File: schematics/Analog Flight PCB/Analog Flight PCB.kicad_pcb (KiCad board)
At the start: 2 copper layers, 99.1 x 56.4 mm, 79 parts, among them J1 Conn_01x02_Male, J10 Conn_01x02_Male, J11 Conn_01x02_Male, J12 Conn_01x02_Male, J2 Conn_01x03_Male, J3 Conn_01x03_Male, J4 Conn_01x03_Male, J5 Conn_01x05_Male, J6 Conn_01x02_Male, J7 Conn_01x02_Male, J8 Conn_01x02_Male, J9 Conn_02x06_Top_Bottom, U1 MAX31856, U2 ADS1115IDGS, U3 NAU7802SGI, U4 MAX31856, U5 MAX31856, U6 MAX31856, U7 MAX31856, U8 MAX31856, U9 LP2985-3.3

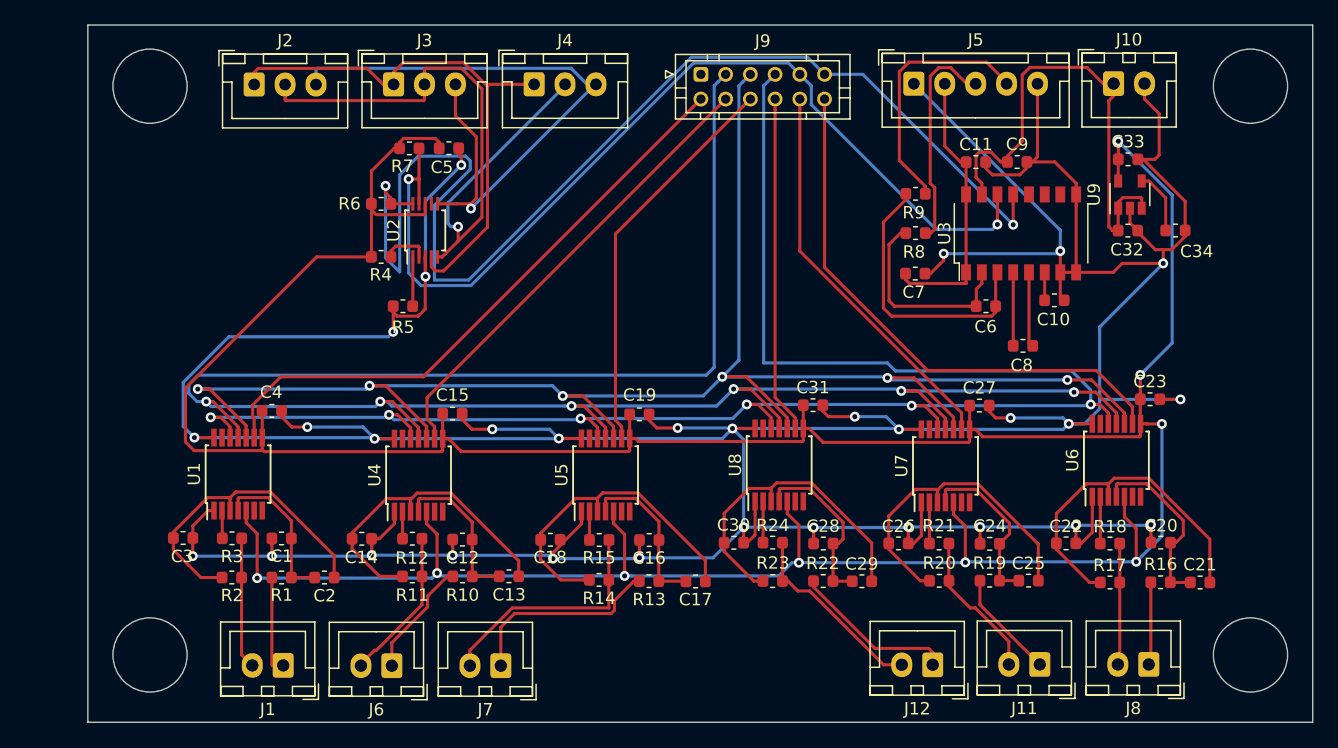
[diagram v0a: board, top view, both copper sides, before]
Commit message: ASPCB: Revision 1.0c
Changed all single row plug connectors to JST-PH instead of JST-XH to
save space. All routes were optimized to place passives closer to ICs
and contacts. Two additional LC reader assemblies were added for test
config. Testpoints have been added on both 3v3 and 5v power supplies for
testing. Power and ground have been moved into primary connector, with
interleaving to preserve signal integrity. First attempt at a ground
plane was implemented. Graphics have been added to silkscreen, and
date/revision info have been added to silkscreen. Parts have been
renumbered for clarity where applicable.
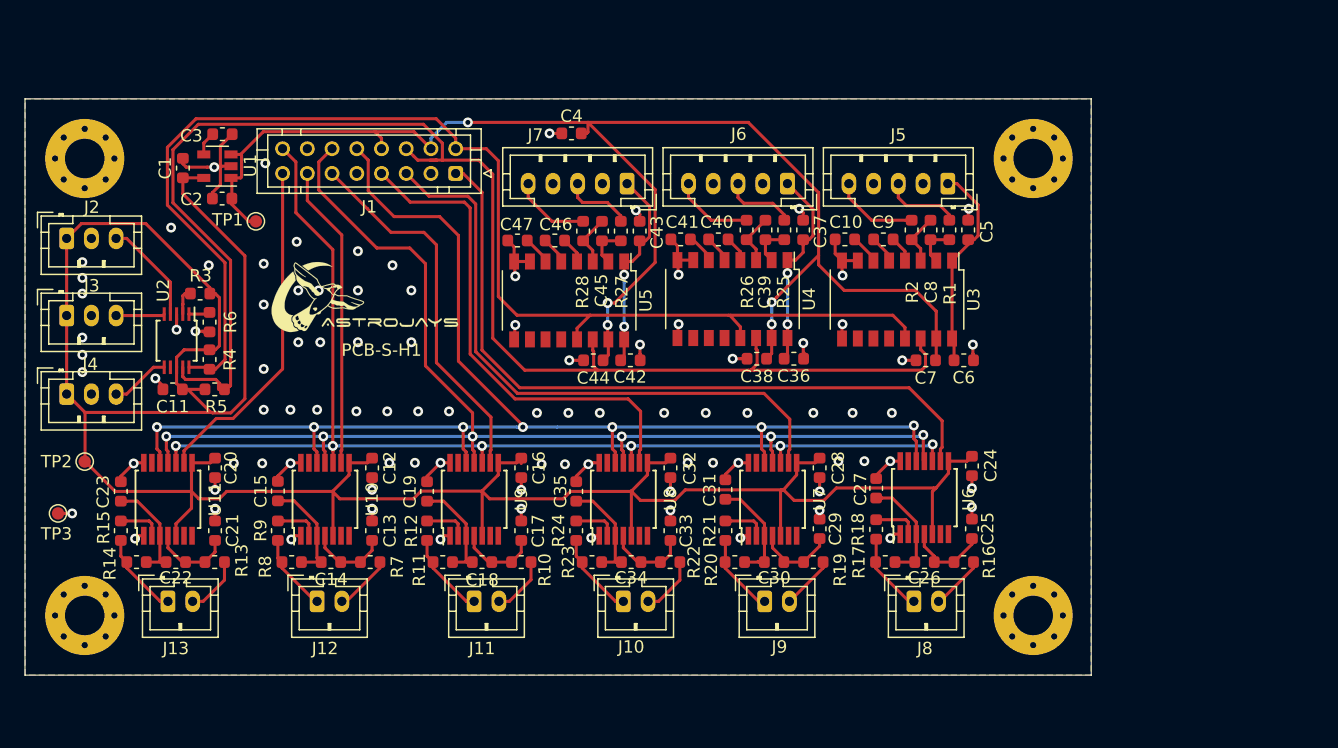
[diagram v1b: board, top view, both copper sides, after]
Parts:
- removed the J10 at (176.4, 71.8)
- removed the J9 at (143.1, 71.0)
- added C36: 0.1u, Capacitor_SMD:C_0603_1608Metric, F.Cu at (150.6, 94.0)
- added C37: 1u, Capacitor_SMD:C_0603_1608Metric, F.Cu at (151.3, 83.6)
- added C38: 1u, Capacitor_SMD:C_0603_1608Metric, F.Cu at (147.6, 94.0)
- added C39: 0.1u, Capacitor_SMD:C_0603_1608Metric, F.Cu at (148.3, 83.6)
- added C4: 10u, Capacitor_SMD:C_0603_1608Metric, F.Cu at (132.6, 75.8)
- added C40: 680p, Capacitor_SMD:C_0603_1608Metric, F.Cu at (144.5, 84.4)
- added C41: 0.1u, Capacitor_SMD:C_0603_1608Metric, F.Cu at (141.4, 84.4)
- added C42: 0.1u, Capacitor_SMD:C_0603_1608Metric, F.Cu at (137.3, 94.2)
- added C43: 1u, Capacitor_SMD:C_0603_1608Metric, F.Cu at (138.1, 83.7)
- added C44: 1u, Capacitor_SMD:C_0603_1608Metric, F.Cu at (134.4, 94.2)
- added C45: 0.1u, Capacitor_SMD:C_0603_1608Metric, F.Cu at (135.1, 83.7)
- added C46: 680p, Capacitor_SMD:C_0603_1608Metric, F.Cu at (131.2, 84.5)
- added C47: 0.1u, Capacitor_SMD:C_0603_1608Metric, F.Cu at (128.2, 84.5)
- added G***: LOGO, AJ_GFX:full_logo_21.3mmx9.3mm, F.Cu at (117.5, 88.8)
- added G***: LOGO, AJ_GFX:small_logo_5.71mmx5.71mm, B.Cu at (152.8, 106.8)
- added J1: Conn_02x08_Odd_Even, Connector_JST:JST_PHD_B16B-PHDSS_2x08_P2.00mm_Vertical, F.Cu at (123.2, 79.1)
- added J6: Conn_01x05_Male, Connector_JST:JST_PH_B5B-PH-K_1x05_P2.00mm_Vertical, F.Cu at (150.1, 79.9)
- added J7: Conn_01x05_Male, Connector_JST:JST_PH_B5B-PH-K_1x05_P2.00mm_Vertical, F.Cu at (137.1, 79.9)
- added M1: MountingHole_3.2mm_M3_Pad_Via, MountingHole:MountingHole_3.2mm_M3_Pad_Via, F.Cu at (93.2, 114.8)
- added M2: MountingHole_3.2mm_M3_Pad_Via, MountingHole:MountingHole_3.2mm_M3_Pad_Via, F.Cu at (93.2, 77.9)
- added M3: MountingHole_3.2mm_M3_Pad_Via, MountingHole:MountingHole_3.2mm_M3_Pad_Via, F.Cu at (169.9, 77.9)
- added M4: MountingHole_3.2mm_M3_Pad_Via, MountingHole:MountingHole_3.2mm_M3_Pad_Via, F.Cu at (169.9, 114.8)
- added R25: 47, Resistor_SMD:R_0603_1608Metric, F.Cu at (149.8, 83.6)
- added R26: 47, Resistor_SMD:R_0603_1608Metric, F.Cu at (146.7, 83.6)
- added R27: 47, Resistor_SMD:R_0603_1608Metric, F.Cu at (136.6, 83.7)
- added R28: 47, Resistor_SMD:R_0603_1608Metric, F.Cu at (133.5, 83.7)
- added TP1: TestPoint, TestPoint:TestPoint_Pad_D1.0mm, F.Cu at (107.1, 82.9)
- added TP2: TestPoint, TestPoint:TestPoint_Pad_D1.0mm, F.Cu at (93.2, 102.4)
- added TP3: TestPoint, TestPoint:TestPoint_Pad_D1.0mm, F.Cu at (91.1, 106.6)
- added U4: NAU7802SGI, Package_SO:SOP-16_4.4x10.4mm_P1.27mm, F.Cu at (145.6, 89.2)
- added U5: NAU7802SGI, Package_SO:SOP-16_4.4x10.4mm_P1.27mm, F.Cu at (132.4, 89.3)
- J10: renamed from J7; footprint Connector_JST:JST_XH_B2B-XH-A_1x02_P2.50mm_Vertical -> Connector_JST:JST_PH_B2B-PH-K_1x02_P2.00mm_Vertical
- J11: renamed from J8; footprint Connector_JST:JST_XH_B2B-XH-A_1x02_P2.50mm_Vertical -> Connector_JST:JST_PH_B2B-PH-K_1x02_P2.00mm_Vertical
- J12: renamed from J11; footprint Connector_JST:JST_XH_B2B-XH-A_1x02_P2.50mm_Vertical -> Connector_JST:JST_PH_B2B-PH-K_1x02_P2.00mm_Vertical
- J13: renamed from J12; footprint Connector_JST:JST_XH_B2B-XH-A_1x02_P2.50mm_Vertical -> Connector_JST:JST_PH_B2B-PH-K_1x02_P2.00mm_Vertical
- J2, J3, J4: footprint Connector_JST:JST_XH_B3B-XH-A_1x03_P2.50mm_Vertical -> Connector_JST:JST_PH_B3B-PH-K_1x03_P2.00mm_Vertical
- J5: footprint Connector_JST:JST_XH_B5B-XH-A_1x05_P2.50mm_Vertical -> Connector_JST:JST_PH_B5B-PH-K_1x05_P2.00mm_Vertical
- J8: renamed from J1; footprint Connector_JST:JST_XH_B2B-XH-A_1x02_P2.50mm_Vertical -> Connector_JST:JST_PH_B2B-PH-K_1x02_P2.00mm_Vertical
- J9: renamed from J6; footprint Connector_JST:JST_XH_B2B-XH-A_1x02_P2.50mm_Vertical -> Connector_JST:JST_PH_B2B-PH-K_1x02_P2.00mm_Vertical
- moved C3 77.5 mm to (104.4, 75.9)
- moved C1 76.4 mm to (101.2, 78.6), turned to 90 degrees
- moved U1 73.8 mm to (103.9, 78.5), turned to 180 degrees
- moved C2 73.3 mm to (104.3, 81.1), turned to 180 degrees
- moved J13 62.1 mm to (99.9, 113.7), turned to 0 degrees
- moved J12 58.7 mm to (112.0, 113.7), turned to 0 degrees
- moved C18 58.1 mm to (125.3, 110.5), turned to 180 degrees
- moved C24 56.8 mm to (165.0, 102.7), turned to 270 degrees
- moved C14 56.4 mm to (113.1, 110.5), turned to 180 degrees
- moved C27 56.2 mm to (157.2, 104.5), turned to 90 degrees
- moved C25 55.8 mm to (165.0, 107.8), turned to 270 degrees
- moved U6 55.5 mm to (161.1, 105.3)
- moved C22 55.5 mm to (100.6, 110.5), turned to 180 degrees
- moved R12 55.2 mm to (120.9, 108.0), turned to 270 degrees
- moved R16 55.2 mm to (164.3, 110.5), turned to 180 degrees
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- renumbered C33 to C1, C5 to C11, C27 to C12, C24 to C13, C25 to C14, C26 to C15, C23 to C16, C20 to C17, C21 to C18, C22 to C19, C32 to C2, C31 to C20, C28 to C21, C29 to C22, C30 to C23, C4 to C24, C1 to C25, C2 to C26, C3 to C27, C15 to C28, C12 to C29, C34 to C3, C13 to C30, C14 to C31, C19 to C32, C16 to C33, C17 to C34, C18 to C35, C7 to C5, C11 to C6, C9 to C7, C6 to C8, C8 to C9, R8 to R1, R16 to R10, R17 to R11, R18 to R12, R22 to R13, R23 to R14, R24 to R15, R1 to R16, R2 to R17, R3 to R18, R10 to R19, R9 to R2, R11 to R20, R12 to R21, R13 to R22, R14 to R23, R15 to R24, R4 to R3, R6 to R4, R7 to R5, R5 to R6, R19 to R7, R20 to R8, R21 to R9, U9 to U1, U7 to U10, U8 to U11, U1 to U6, U4 to U7, U5 to U8, U6 to U9
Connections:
- net /LC/SCL renamed /I2C1_SCL
- net /LC/SDA renamed /I2C1_SDA
- net /tc1/SCK renamed /SPI1_SCK
- net /tc1/SDI renamed /SPI1_SDI
- net /tc1/SDO renamed /SPI1_SDO
- C5 pad 1: Net-(C11-Pad1) -> Net-(C5-Pad1)
- C6 pad 1: Net-(C11-Pad1) -> Net-(C5-Pad1)
- J10 pad 1: Net-(J7-Pad1) -> Net-(J10-Pad1)
- J10 pad 2: Net-(J7-Pad2) -> Net-(J10-Pad2)
- J11 pad 1: Net-(J8-Pad1) -> Net-(J11-Pad1)
- J11 pad 2: Net-(J8-Pad2) -> Net-(J11-Pad2)
- J12 pad 1: Net-(J11-Pad1) -> Net-(J12-Pad1)
- J12 pad 2: Net-(J11-Pad2) -> Net-(J12-Pad2)
- J13 pad 1: Net-(J12-Pad1) -> Net-(J13-Pad1)
- J13 pad 2: Net-(J12-Pad2) -> Net-(J13-Pad2)
- J2 pad 1: Net-(J2-Pad1) -> +3V3
- J2 pad 2: Net-(J2-Pad2) -> GND
- J3 pad 1: Net-(J2-Pad1) -> +3V3
- J3 pad 2: Net-(J2-Pad2) -> GND
- J3 pad 3: Net-(J2-Pad3) -> Net-(J3-Pad3)
- J4 pad 1: Net-(J2-Pad1) -> +3V3
- J4 pad 2: Net-(J2-Pad2) -> GND
- J4 pad 3: Net-(J2-Pad3) -> Net-(J4-Pad3)
- J5 pad 1: GND -> Net-(C5-Pad1)
- J5 pad 2: Net-(C11-Pad1) -> GND
- J5 pad 4: Net-(J5-Pad4) -> GND
- J5 pad 5: GND -> Net-(J5-Pad5)
- J8 pad 1: Net-(J1-Pad1) -> Net-(J8-Pad1)
- J8 pad 2: Net-(J1-Pad2) -> Net-(J8-Pad2)
- J9 pad 1: Net-(J6-Pad1) -> Net-(J9-Pad1)
- J9 pad 2: Net-(J6-Pad2) -> Net-(J9-Pad2)
- R10 pad 1: Net-(J8-Pad1) -> Net-(J11-Pad2)
- R11 pad 2: Net-(J8-Pad2) -> Net-(J11-Pad1)
- R12 pad 2: Net-(J8-Pad2) -> Net-(J11-Pad1)
- R13 pad 1: Net-(J12-Pad1) -> Net-(J13-Pad2)
- R14 pad 2: Net-(J12-Pad2) -> Net-(J13-Pad1)
- R15 pad 2: Net-(J12-Pad2) -> Net-(J13-Pad1)
- R16 pad 1: Net-(J1-Pad1) -> Net-(J8-Pad2)
- R17 pad 2: Net-(J1-Pad2) -> Net-(J8-Pad1)
- R18 pad 2: Net-(J1-Pad2) -> Net-(J8-Pad1)
- R19 pad 1: Net-(J6-Pad1) -> Net-(J9-Pad2)
- R2 pad 2: Net-(J5-Pad4) -> Net-(J5-Pad5)
- R20 pad 2: Net-(J6-Pad2) -> Net-(J9-Pad1)
- R21 pad 2: Net-(J6-Pad2) -> Net-(J9-Pad1)
- R22 pad 1: Net-(J7-Pad1) -> Net-(J10-Pad2)
- R23 pad 2: Net-(J7-Pad2) -> Net-(J10-Pad1)
- R24 pad 2: Net-(J7-Pad2) -> Net-(J10-Pad1)
- R7 pad 1: Net-(J11-Pad1) -> Net-(J12-Pad2)
- R8 pad 2: Net-(J11-Pad2) -> Net-(J12-Pad1)
- R9 pad 2: Net-(J11-Pad2) -> Net-(J12-Pad1)
- U2 pad 4: Net-(J2-Pad1) -> Net-(J2-Pad3)
- U2 pad 5: Net-(J2-Pad2) -> Net-(J3-Pad3)
- U2 pad 6: Net-(J2-Pad3) -> Net-(J4-Pad3)
- U3 pad 1: Net-(C11-Pad1) -> Net-(C5-Pad1)
- U3 pad 16: Net-(C11-Pad1) -> Net-(C5-Pad1)
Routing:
- net GND: track 410.4 -> 75.6 mm, vias 30 -> 94
- net +3V3: track 286.4 -> 208.3 mm, vias 9 -> 0
- net +5V: track 39.8 -> 117.3 mm, vias 0 -> 5
- net /SPI1_SDO: track 170.3 -> 103.8 mm
- net Net-(J2-Pad2): track 53.0 -> 0.00 mm, vias 1 -> 0
- net Net-(J2-Pad1): track 44.8 -> 0.00 mm
- net Net-(J2-Pad3): track 52.3 -> 8.44 mm, vias 1 -> 0
- net /SPI1_SCK: track 137.8 -> 95.2 mm
- net /I2C1_SDA: track 77.5 -> 116.8 mm, vias 2 -> 0
- net /SPI1_SDI: track 141.9 -> 108.8 mm, vias 6 -> 7
- net Net-(C11-Pad1): track 22.6 -> 0.00 mm
- net Net-(J5-Pad4): track 20.5 -> 0.00 mm
- net Net-(J7-Pad2): track 19.4 -> 0.00 mm
- net Net-(C18-Pad2): track 27.8 -> 8.64 mm
- net Net-(C8-Pad2): track 22.7 -> 4.20 mm
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- added copper zone on B.Cu, net GND
- added copper zone on F.Cu, net GND
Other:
- board size 99.1 x 56.4 mm -> 86.2 x 46.6 mm
- board text added: "DAQ Sensors PCB - Rev 1.0c Part ID: PCB-S-H1 Astrojays Rocketry JHU, Jan 2020"
- board text added: "PCB-S-H1"

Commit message: ASPCB: Rev 1.0d
Added three new TC ADCs per prop request. Loadcell interfaces had
conflicting I2C addresses so a TI PCA9548 8ch I2C switch was added.
PT supply voltage was changed from 3V3 to 5V. I2C level shifter using
MOSFETs per Phillips AN97055 was added to ensure I2C bus reliability.
Extra 5V power supply pin removed since one pin supplies up to 1A, far
above the max current draw of this board. Traces have been rerouted for
noise.
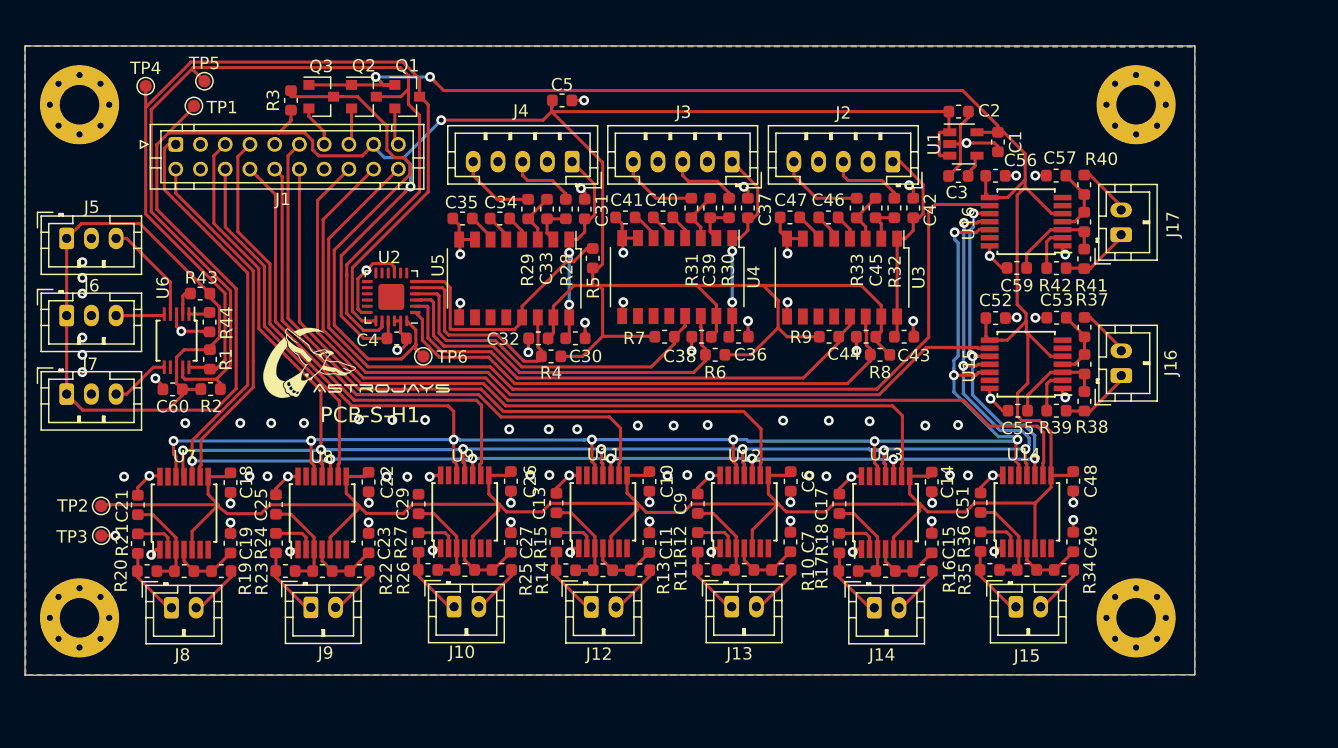
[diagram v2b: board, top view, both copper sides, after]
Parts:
- added C4: 1u, Capacitor_SMD:C_0603_1608Metric, F.Cu at (118.5, 92.4)
- added C48: 0.1u, Capacitor_SMD:C_0603_1608Metric, F.Cu at (173.2, 103.9)
- added C49: 0.01u, Capacitor_SMD:C_0603_1608Metric, F.Cu at (173.2, 108.9)
- added C50: 0.1u, Capacitor_SMD:C_0603_1608Metric, F.Cu at (169.4, 111.1)
- added C51: 0.01u, Capacitor_SMD:C_0603_1608Metric, F.Cu at (165.7, 105.7)
- added C52: 0.1u, Capacitor_SMD:C_0603_1608Metric, F.Cu at (166.9, 90.8)
- added C53: 0.01u, Capacitor_SMD:C_0603_1608Metric, F.Cu at (171.8, 90.7)
- added C54: 0.1u, Capacitor_SMD:C_0603_1608Metric, F.Cu at (174.1, 94.5)
- added C55: 0.01u, Capacitor_SMD:C_0603_1608Metric, F.Cu at (168.7, 98.2)
- added C56: 0.1u, Capacitor_SMD:C_0603_1608Metric, F.Cu at (166.9, 79.2)
- added C57: 0.01u, Capacitor_SMD:C_0603_1608Metric, F.Cu at (171.8, 79.2)
- added C58: 0.1u, Capacitor_SMD:C_0603_1608Metric, F.Cu at (174.1, 83.0)
- added C59: 0.01u, Capacitor_SMD:C_0603_1608Metric, F.Cu at (168.6, 86.7)
- added J15: Conn_01x02_Male, Connector_JST:JST_PH_B2B-PH-K_1x02_P2.00mm_Vertical, F.Cu at (168.5, 114.1)
- added J16: Conn_01x02_Male, Connector_JST:JST_PH_B2B-PH-K_1x02_P2.00mm_Vertical, F.Cu at (177.1, 95.4)
- added J17: Conn_01x02_Male, Connector_JST:JST_PH_B2B-PH-K_1x02_P2.00mm_Vertical, F.Cu at (177.0, 84.0)
- added Q1: BSS138, Package_TO_SOT_SMD:SOT-23, F.Cu at (119.3, 72.8)
- added Q2: BSS138, Package_TO_SOT_SMD:SOT-23, F.Cu at (115.8, 72.8)
- added Q3: BSS138, Package_TO_SOT_SMD:SOT-23, F.Cu at (112.3, 72.8)
- added R1: 10k, Resistor_SMD:R_0603_1608Metric, F.Cu at (103.3, 94.1)
- added R2: 10k, Resistor_SMD:R_0603_1608Metric, F.Cu at (103.4, 96.5)
- added R3: 10k, Resistor_SMD:R_0603_1608Metric, F.Cu at (109.9, 73.2)
- added R34: 2k, Resistor_SMD:R_0603_1608Metric, F.Cu at (172.4, 111.1)
- added R35: 2k, Resistor_SMD:R_0603_1608Metric, F.Cu at (166.4, 111.1)
- added R36: 2k, Resistor_SMD:R_0603_1608Metric, F.Cu at (165.7, 108.8)
- added R37: 2k, Resistor_SMD:R_0603_1608Metric, F.Cu at (174.1, 91.5)
- added R38: 2k, Resistor_SMD:R_0603_1608Metric, F.Cu at (174.1, 97.5)
- added R39: 2k, Resistor_SMD:R_0603_1608Metric, F.Cu at (171.8, 98.2)
- added R40: 2k, Resistor_SMD:R_0603_1608Metric, F.Cu at (174.1, 80.0)
- added R41: 2k, Resistor_SMD:R_0603_1608Metric, F.Cu at (174.1, 86.0)
- added R42: 2k, Resistor_SMD:R_0603_1608Metric, F.Cu at (171.8, 86.7)
- added R6: 10k, Resistor_SMD:R_0603_1608Metric, F.Cu at (144.2, 93.7)
- added R7: 10k, Resistor_SMD:R_0603_1608Metric, F.Cu at (140.1, 92.3)
- added R8: 10k, Resistor_SMD:R_0603_1608Metric, F.Cu at (157.5, 93.7)
- added R9: 10k, Resistor_SMD:R_0603_1608Metric, F.Cu at (153.4, 92.3)
- added TP4: TP_5V_I2C1_SCL, TestPoint:TestPoint_Pad_D1.0mm, F.Cu at (98.2, 72.0)
- added TP5: TP_5V_I2C1_SDA, TestPoint:TestPoint_Pad_D1.0mm, F.Cu at (102.9, 71.6)
- added TP6: TP_5V_I2C1_RST, TestPoint:TestPoint_Pad_D1.0mm, F.Cu at (120.6, 93.8)
- added U14: MAX31856, Package_SO:TSSOP-14_4.4x5mm_P0.65mm, F.Cu at (169.4, 106.4)
- added U15: MAX31856, Package_SO:TSSOP-14_4.4x5mm_P0.65mm, F.Cu at (169.4, 94.5)
- added U16: MAX31856, Package_SO:TSSOP-14_4.4x5mm_P0.65mm, F.Cu at (169.4, 83.0)
- added U2: PCA9548ARGE, Package_DFN_QFN:Texas_RGE0024C_EP2.1x2.1mm, F.Cu at (118.0, 89.0)
- J1: value Conn_02x08_Odd_Even -> 20-Pin Interconnect; footprint Connector_JST:JST_PHD_B16B-PHDSS_2x08_P2.00mm_Vertical -> Connector_JST:JST_PHD_B20B-PHDSS_2x10_P2.00mm_Vertical
- TP1: value TestPoint -> TP_5V
- TP2: value TestPoint -> TP_3V3
- TP3: value TestPoint -> TP_GND
- U6: renamed from U2; value ADS1115IDGS -> ADS1015IDGS
- moved C1 66.0 mm to (167.1, 76.5), turned to 270 degrees
- moved U1 60.4 mm to (164.3, 76.7), turned to 0 degrees
- moved R19 60.1 mm to (104.3, 111.2)
- moved J8 60.0 mm to (100.2, 114.2)
- moved C2 60.0 mm to (163.9, 74.1), turned to 0 degrees
- moved C18 60.0 mm to (105.0, 104.1)
- moved C19 60.0 mm to (105.0, 109.0)
- moved U7 59.9 mm to (101.3, 106.5)
- moved C20 59.9 mm to (101.3, 111.2)
- moved C21 59.7 mm to (97.5, 105.9)
- moved R21 59.7 mm to (97.5, 109.0)
- moved R20 59.7 mm to (98.3, 111.2)
- moved C3 59.6 mm to (163.9, 79.3), turned to 180 degrees
- moved C17 58.1 mm to (154.3, 105.8)
- moved R18 58.1 mm to (154.3, 109.0)
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- renumbered C16 to C10, C17 to C11, C18 to C12, C19 to C13, C20 to C14, C21 to C15, C22 to C16, C23 to C17, C24 to C18, C25 to C19, C26 to C20, C27 to C21, C28 to C22, C29 to C23, C30 to C24, C31 to C25, C32 to C26, C33 to C27, C34 to C28, C35 to C29, C42 to C30, C43 to C31, C44 to C32, C45 to C33, C46 to C34, C47 to C35, C5 to C42, C6 to C43, C7 to C44, C8 to C45, C9 to C46, C10 to C47, C4 to C5, C12 to C6, C11 to C60, C13 to C7, C14 to C8, C15 to C9, J11 to J12, J12 to J13, J13 to J14, J5 to J2, J6 to J3, J7 to J4, J2 to J5, J3 to J6, J4 to J7, R7 to R10, R8 to R11, R9 to R12, R10 to R13, R11 to R14, R12 to R15, R13 to R16, R14 to R17, R15 to R18, R16 to R19, R17 to R20, R18 to R21, R19 to R22, R20 to R23, R21 to R24, R22 to R25, R23 to R26, R24 to R27, R27 to R28, R28 to R29, R25 to R30, R26 to R31, R1 to R32, R2 to R33, R3 to R43, R6 to R44, U9 to U11, U10 to U12, U11 to U13, U6 to U7, U7 to U8, U8 to U9
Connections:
- net Net-(U3-Pad12) renamed /LC1/DRDY
- net Net-(U4-Pad12) renamed /LC2/DRDY
- net Net-(U5-Pad12) renamed /LC3/DRDY
- C60 pad 1: +3V3 -> +5V
- J1 pad 1: /tc1/CS -> /SPI1_SCK
- J1 pad 10: /SPI1_SDI -> /SPI1_CS4
- J1 pad 11: /tc4/CS -> /SPI1_CS5
- J1 pad 12: /SPI1_SDO -> /SPI1_CS6
- J1 pad 13: /tc5/CS -> /3V3_I2C1_RESET
- J1 pad 15: /tc6/CS -> /3V3_I2C1_SDA
- J1 pad 16: /SPI1_SCK -> /SPI1_CS7
- J1 pad 2: /I2C1_SCL -> /SPI1_CS1
- J1 pad 4: +5V -> GND
- J1 pad 5: /tc2/CS -> /SPI1_SDO
- J1 pad 6: /I2C1_SDA -> /SPI1_CS2
- J1 pad 7: /tc3/CS -> /SPI1_SDI
- J1 pad 8: +5V -> /SPI1_CS3
- J5 pad 1: +3V3 -> +5V
- J6 pad 1: +3V3 -> +5V
- J7 pad 1: +3V3 -> +5V
- R4 pad 1: +3V3 -> +5V
- R4 pad 2: /I2C1_SCL -> /LC3_SDA
- R43 pad 1: +3V3 -> +5V
- R5 pad 1: +3V3 -> +5V
- R5 pad 2: /I2C1_SDA -> /LC3_SCL
- U11 pad 9: /tc4/CS -> /SPI1_CS4
- U12 pad 9: /tc5/CS -> /SPI1_CS5
- U13 pad 9: /tc6/CS -> /SPI1_CS6
- U3 pad 13: /I2C1_SCL -> /LC1_SCL
- U3 pad 14: /I2C1_SDA -> /LC1_SDA
- U4 pad 13: /I2C1_SCL -> /LC2_SCL
- U4 pad 14: /I2C1_SDA -> /LC2_SDA
- U5 pad 13: /I2C1_SCL -> /LC3_SCL
- U5 pad 14: /I2C1_SDA -> /LC3_SDA
- U6 pad 10: /I2C1_SCL -> /5V_I2C1_SCL
- U6 pad 8: +3V3 -> +5V
- U6 pad 9: /I2C1_SDA -> /5V_I2C1_SDA
- U7 pad 9: /tc1/CS -> /SPI1_CS1
- U8 pad 9: /tc2/CS -> /SPI1_CS2
- U9 pad 9: /tc3/CS -> /SPI1_CS3
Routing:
- net +5V: track 117.3 -> 264.4 mm, vias 5 -> 2
- net /I2C1_SDA: track 116.8 -> 0.00 mm
- net /I2C1_SCL: track 102.4 -> 0.00 mm
- net /SPI1_CS9: track 0.00 -> 82.9 mm
- net /5V_I2C1_SDA: track 0.00 -> 82.5 mm
- net /SPI1_CS7: track 0.00 -> 79.8 mm
- net /5V_I2C1_SCL: track 0.00 -> 76.2 mm
- net /SPI1_CS8: track 0.00 -> 72.4 mm
- net /SPI1_CS6: track 0.00 -> 69.2 mm
- net /SPI1_CS5: track 0.00 -> 60.5 mm
- net /tc1/CS: track 58.4 -> 0.00 mm
- net /tc2/CS: track 49.8 -> 0.00 mm
- net /SPI1_CS4: track 0.00 -> 47.3 mm
- net +3V3: track 208.3 -> 255.6 mm, vias 0 -> 2
- net /LC1_SDA: track 0.00 -> 44.7 mm
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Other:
- board size 86.2 x 46.6 mm -> 94.6 x 50.9 mm
- board text added: "DAQ Sensors PCB - Rev 1.0d Part ID: PCB-S-H1 Astrojays Rocketry JHU, Jan 2020"
- board text removed: "DAQ Sensors PCB - Rev 1.0c Part ID: PCB-S-H1 Astrojays Rocketry JHU, Jan 2020"

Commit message: ASPCB: Rev 1.0e
Optimized routing to prevent tombstoning. Analog trace lengths were
further shortened, and extranious traces were removed. uCs have been
renumbered to be fully consecutive.
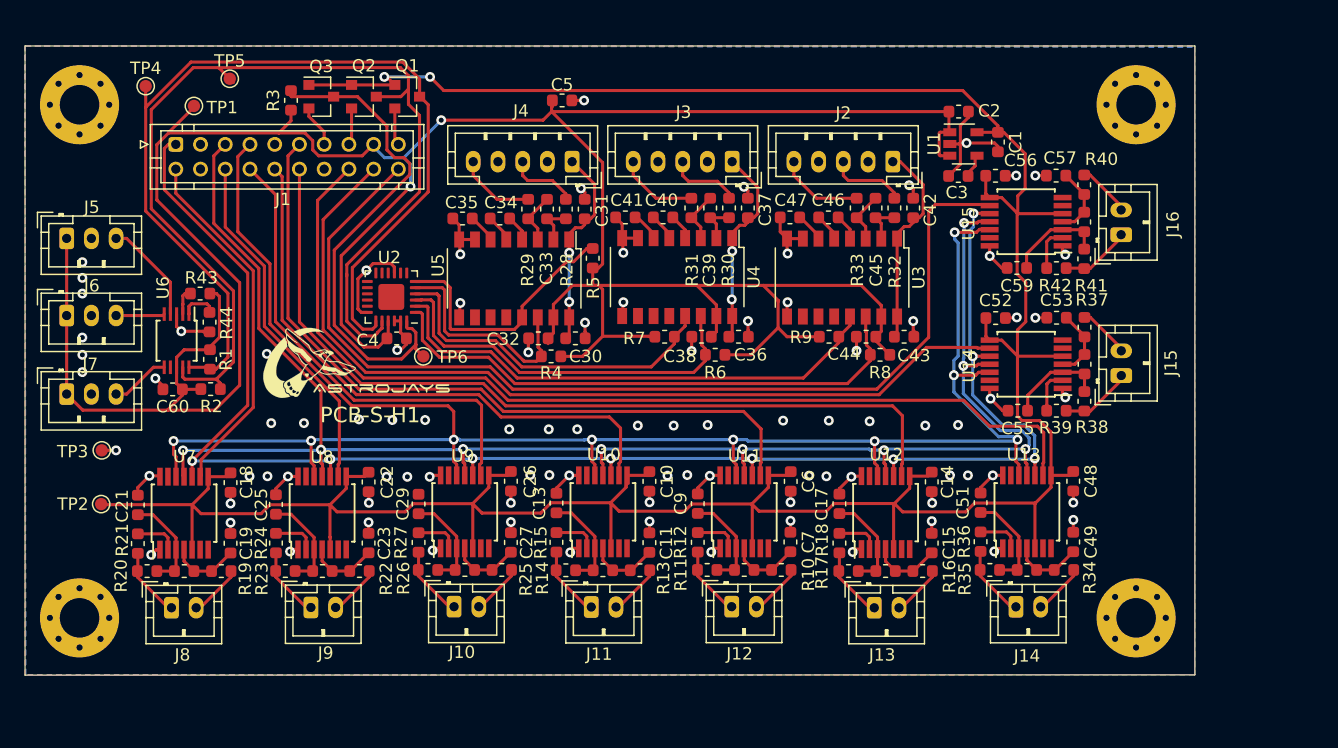
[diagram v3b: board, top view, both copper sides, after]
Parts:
- moved TP3 6.90 mm to (94.6, 101.5)
- moved G*** 3.19 mm to (155.4, 108.7)
- moved TP5 2.06 mm to (105.0, 71.4)
- moved TP2 0.15 mm to (94.5, 105.8)
- renumbered J12 to J11, J13 to J12, J14 to J13, J15 to J14, J16 to J15, J17 to J16, U11 to U10, U12 to U11, U13 to U12, U14 to U13, U15 to U14, U16 to U15
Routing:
- net +5V: track 264.4 -> 251.6 mm
- net +3V3: track 255.6 -> 247.2 mm
- net /5V_I2C1_SCL: track 76.2 -> 77.5 mm
- net /5V_I2C1_SDA: track 82.5 -> 83.7 mm
- net Net-(R44-Pad2): track 1.77 -> 3.00 mm
- net GND: vias 95 -> 93
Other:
- board text added: "DAQ Sensors PCB - Rev 1.0e Part ID: PCB-S-H1 Astrojays Rocketry JHU, Jan 2020"
- board text removed: "DAQ Sensors PCB - Rev 1.0d Part ID: PCB-S-H1 Astrojays Rocketry JHU, Jan 2020"
